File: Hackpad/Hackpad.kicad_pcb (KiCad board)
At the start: 2 copper layers, 4 parts, among them SW1 SW_Push, SW2 SW_Push, SW3 SW_Push, U1 MOUDLE-SEEEDUINO-XIAO

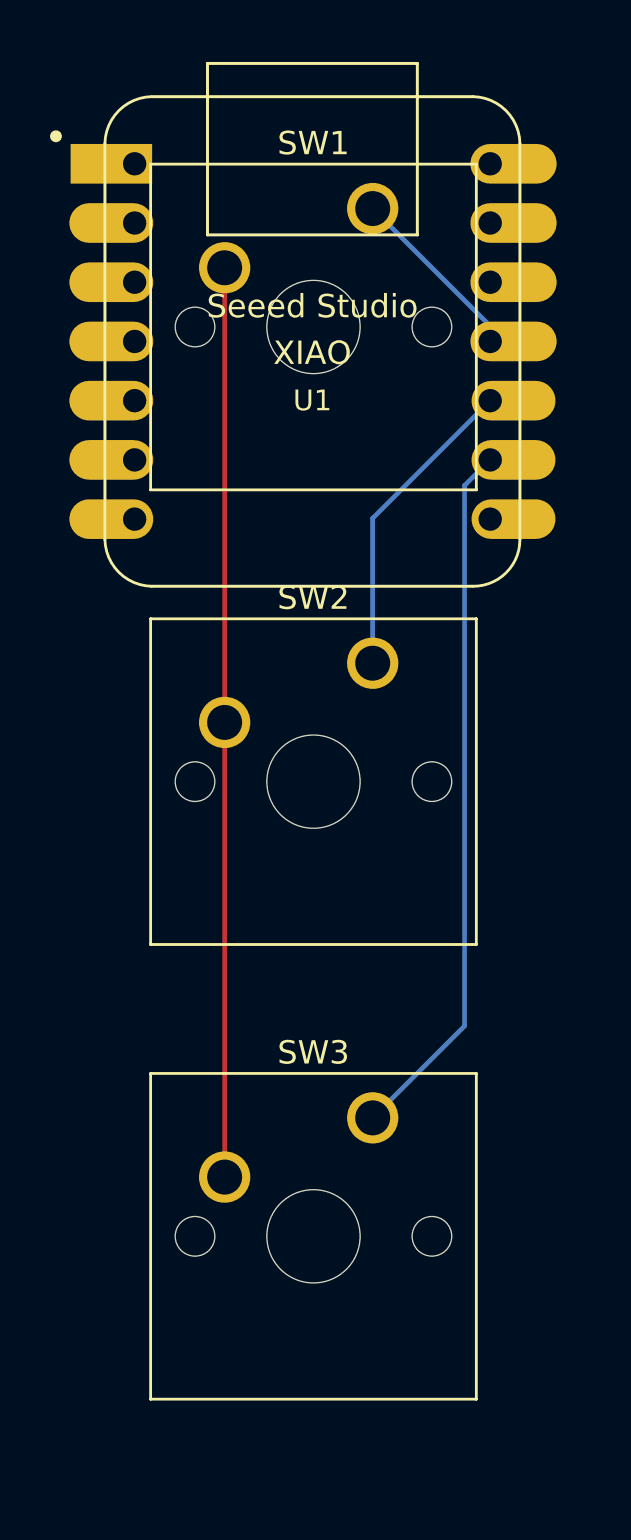
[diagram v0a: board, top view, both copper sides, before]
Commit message: Added case!
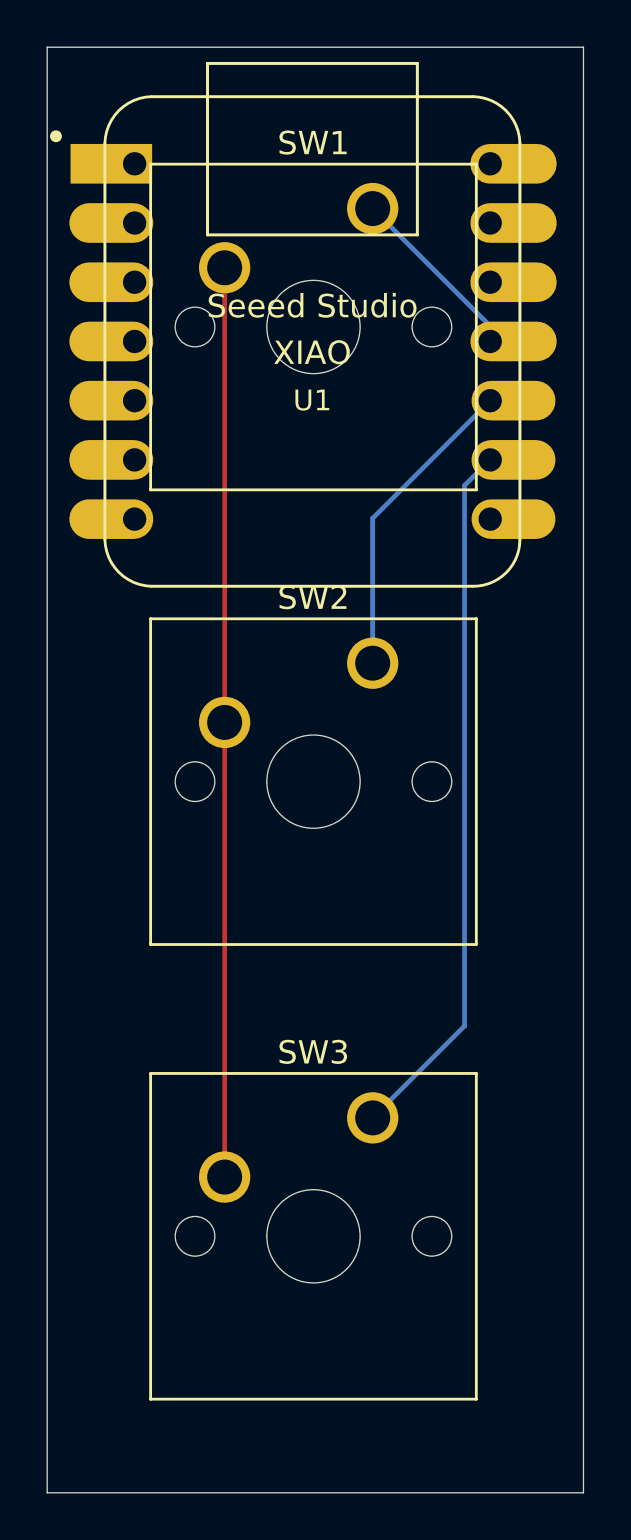
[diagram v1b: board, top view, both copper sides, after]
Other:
- board outline added: 23 x 62 mm
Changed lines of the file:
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@@
 		(embedded_fonts no)
+	)
+	(gr_rect
+		(start 78.5 58.5)
+		(end 101.5 120.5)
+		(stroke
+			(width 0.05)
+			(type default)
+		)
+		(fill no)
+		(layer "Edge.Cuts")
 	)
 	(segment
